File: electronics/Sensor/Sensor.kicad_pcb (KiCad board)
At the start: 2 copper layers, 88 x 59 mm, 11 parts, among them J1 SS-60000-009, J2 SS-60000-009, U1 OPA320AIDBVT, U2 Teensy3.2

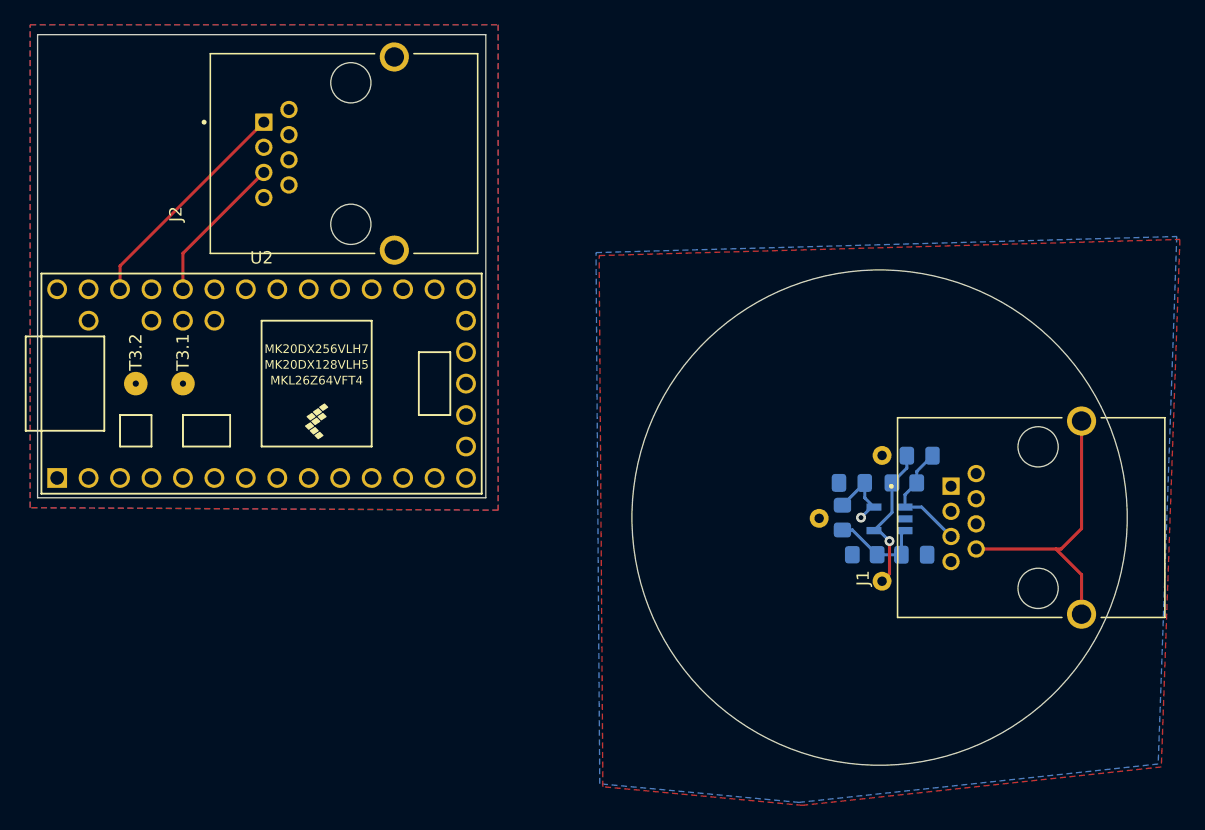
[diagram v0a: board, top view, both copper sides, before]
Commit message: split controller and sensor + add gerbers
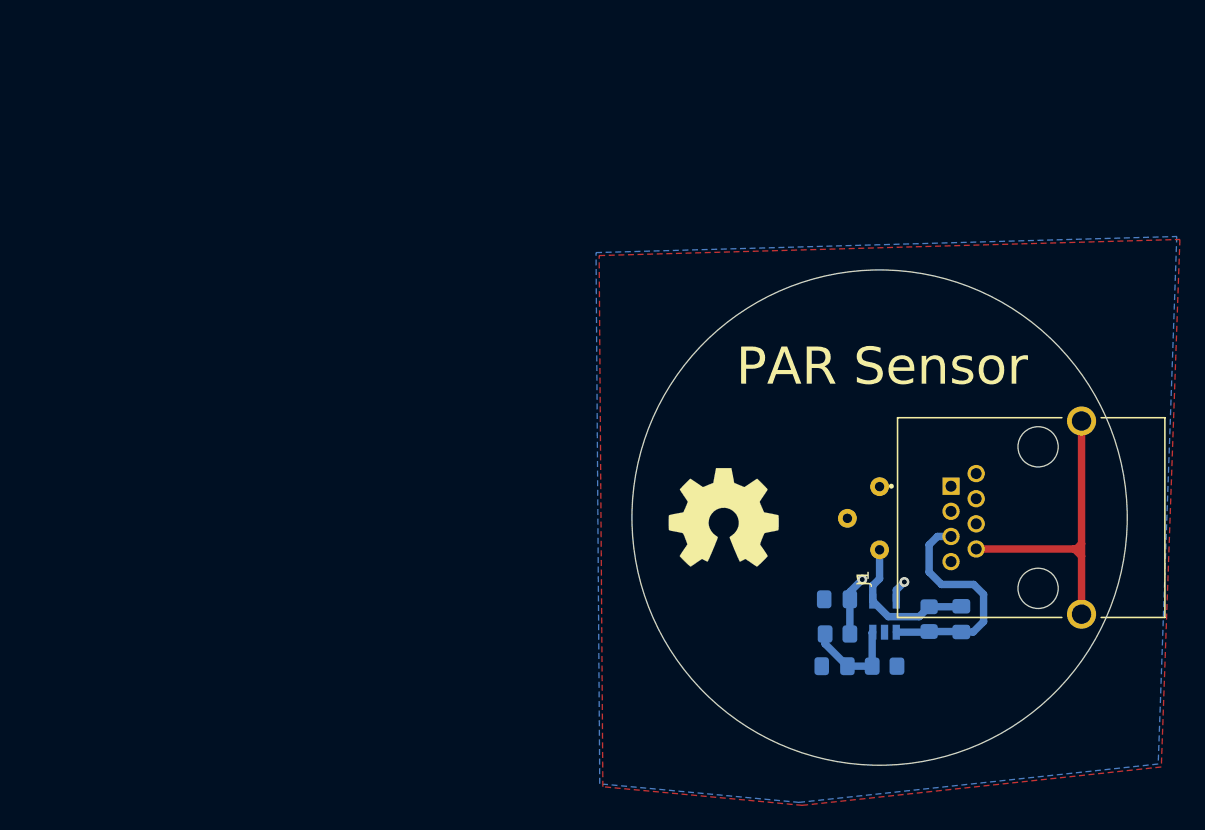
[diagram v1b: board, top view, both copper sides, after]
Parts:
- removed J2: SS-60000-009, ethernet:BEL_SS-60000-009
- removed U2: Teensy3.2, Teensy:Teensy30_31_32_LC
- added REF**: OSHW-Symbol_8.9x8mm_SilkScreen, Symbol:OSHW-Symbol_8.9x8mm_SilkScreen, F.Cu at (198.0, 83.6)
- moved C2 13.6 mm to (217.2, 91.8), turned to 90 degrees
- moved R3 11.2 mm to (214.6, 91.8), turned to 90 degrees
- moved C1 11.1 mm to (207.0, 95.6), turned to 180 degrees
- moved C3 9.48 mm to (207.2, 90.2)
- moved R1 9.41 mm to (207.2, 93.0), turned to 180 degrees
- moved R2 9.14 mm to (211.0, 95.6), turned to 0 degrees
- moved U1 7.91 mm to (211.0, 91.6), turned to 90 degrees
- moved D1 0.20 mm to (210.6, 86.2)
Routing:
- net +3V3: track 18.3 -> 0.00 mm
- net /TeensySide/Fout: track 12.1 -> 0.00 mm
- net /Fout: track 9.77 -> 19.0 mm
- net /SensorGND: track 24.0 -> 25.1 mm
- net /3.3V: track 6.21 -> 6.63 mm, vias 1 -> 2
- net Net-(C2-Pad2): track 12.2 -> 12.4 mm, vias 1 -> 0
- removed copper zone on F.Cu, net GND
- removed copper zone on B.Cu, net GNDA
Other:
- board size 88 x 59 mm -> 40 x 40 mm
- board text added: "PAR Sensor"
